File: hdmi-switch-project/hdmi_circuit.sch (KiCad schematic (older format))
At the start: 18 parts, among them U1 TMDS442_single_unit

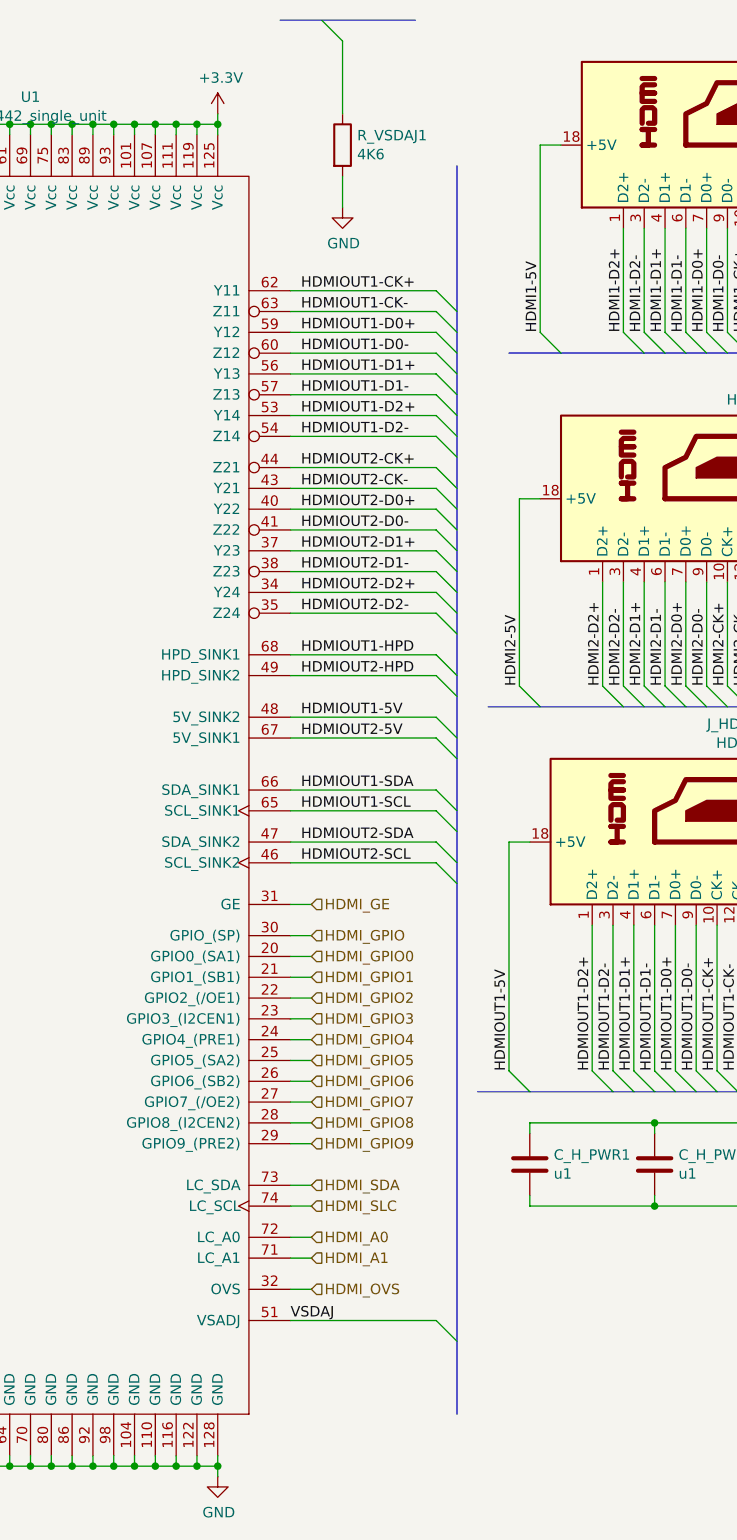
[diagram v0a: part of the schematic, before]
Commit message: Cosmetical changes, and VSDJ pin fixup
Signed-off-by: Andrej Manduch <amanduch@gmail.com>
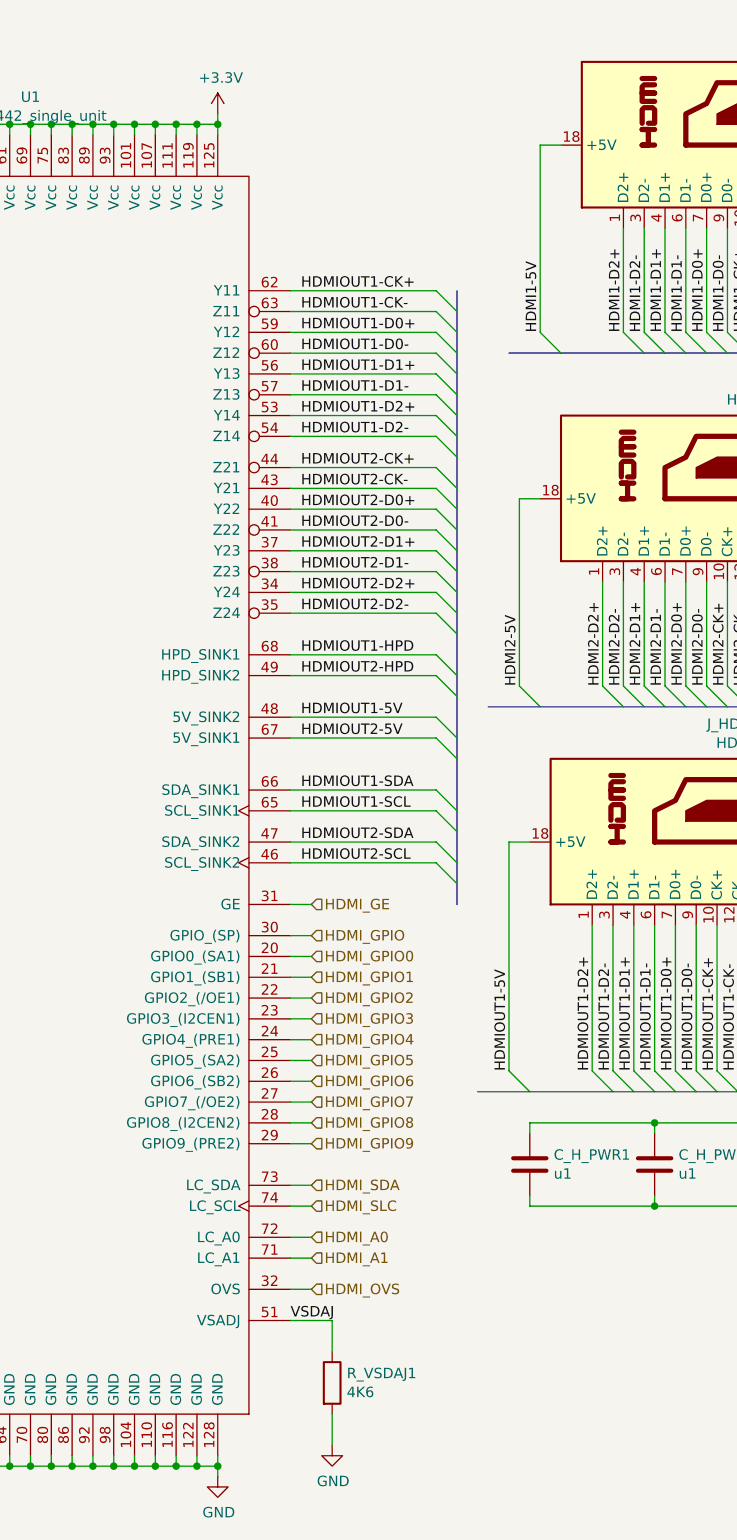
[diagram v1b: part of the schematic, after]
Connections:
- net VSDAJ: now also R_VSDAJ1.1
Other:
- moved on the sheet: R_VSDAJ1
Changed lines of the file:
@@
 encoding utf-8
 Sheet 3 4
-Title ""
-Date ""
+Title "HDMI Switch 4:2 modul"
+Date "2020-06-30"
 Rev ""
 Comp ""
-Comment1 ""
-Comment2 ""
+Comment1 "Devel board"
+Comment2 "HDMI part"
 Comment3 ""
 Comment4 ""
 $EndDescr
 Text GLabel 7400 1450 3    50   Input ~ 0
-SHIELD
-Text GLabel 7300 3150 3    50   Input ~ 0
 SHIELD
 Text GLabel 10200 3100 3    50   Input ~ 0
@@
 Wire Wire Line
 	7300 3050 7300 2950
-Wire Wire Line
-	7300 3150 7300 3050
-Connection ~ 7300 3050
 Wire Wire Line
 	7400 1350 7400 1250
@@
 VSDAJ
 Wire Wire Line
-	3700 6800 4400 6800
+	3700 6800 3900 6800
 Connection ~ 3350 7500
 Wire Wire Line
@@
 Wire Wire Line
 	3350 1050 3350 1000
-Entry Wire Line
-	3850 550  3950 650
-Wire Wire Line
-	3950 650  3950 1000
+Wire Wire Line
+	3900 6800 3900 6950
 $Comp
 L Device:R R_VSDAJ?
 U 1 1 5FA38789
-P 3950 1150
+P 3900 7100
 AR Path="/5FA38789" Ref="R_VSDAJ?"  Part="1"
 AR Path="/5F9FB5DF/5FA38789" Ref="R_VSDAJ1"  Part="1"
-F 0 "R_VSDAJ1" H 4020 1196 50  0000 L CNN
-F 1 "4K6" H 4020 1105 50  0000 L CNN
-F 2 "Resistor_SMD:R_1020_2550Metric" V 3880 1150 50  0001 C CNN
-F 3 "~" H 3950 1150 50  0001 C CNN
-F 4 "Precission" H 3950 1150 50  0001 C CNN "Note"
-	1    3950 1150
+F 0 "R_VSDAJ1" H 3970 7146 50  0000 L CNN
+F 1 "4K6" H 3970 7055 50  0000 L CNN
+F 2 "Resistor_SMD:R_1020_2550Metric" V 3830 7100 50  0001 C CNN
+F 3 "~" H 3900 7100 50  0001 C CNN
+F 4 "Precission" H 3900 7100 50  0001 C CNN "Note"
+	1    3900 7100
 	1    0    0    -1
 $EndComp
@@
 L power:GND #PWR?
 U 1 1 5FA38782
-P 3950 1450
+P 3900 7400
 AR Path="/5FA38782" Ref="#PWR?"  Part="1"
 AR Path="/5F9FB5DF/5FA38782" Ref="#PWR06"  Part="1"
-F 0 "#PWR06" H 3950 1200 50  0001 C CNN
-F 1 "GND" H 3955 1277 50  0000 C CNN
-F 2 "" H 3950 1450 50  0001 C CNN
-F 3 "" H 3950 1450 50  0001 C CNN
-	1    3950 1450
-	1    0    0    -1
-$EndComp
-Wire Wire Line
-	3950 1300 3950 1450
-Entry Wire Line
-	4400 6800 4500 6900
+F 0 "#PWR06" H 3900 7150 50  0001 C CNN
+F 1 "GND" H 3905 7227 50  0000 C CNN
+F 2 "" H 3900 7400 50  0001 C CNN
+F 3 "" H 3900 7400 50  0001 C CNN
+	1    3900 7400
+	1    0    0    -1
+$EndComp
+Wire Wire Line
+	3900 7250 3900 7400
 Connection ~ 10250 6250
 Wire Wire Line
@@
 Connection ~ 9050 5850
 Connection ~ 9050 6250
+Connection ~ 7300 3050
 Wire Bus Line
-	3650 550  4300 550
+	7600 5750 9900 5750
 Wire Bus Line
-	4750 2150 7050 2150
+	550  1500 550  7200
+Wire Bus Line
+	4500 1850 4500 4800
+Wire Bus Line
+	4600 5700 6800 5700
+Wire Bus Line
+	4650 3850 6950 3850
+Wire Bus Line
+	7550 2150 9850 2150
 Wire Bus Line
 	7550 3800 9850 3800
 Wire Bus Line
-	7550 2150 9850 2150
-Wire Bus Line
-	4650 3850 6950 3850
-Wire Bus Line
-	4600 5700 6800 5700
-Wire Bus Line
-	7600 5750 9900 5750
-Wire Bus Line
-	4500 1250 4500 7250
-Wire Bus Line
-	550  1500 550  7200
+	4750 2150 7050 2150
+Wire Wire Line
+	7300 3150 7300 3050
+Text GLabel 7300 3150 3    50   Input ~ 0
+SHIELD
 $EndSCHEMATC

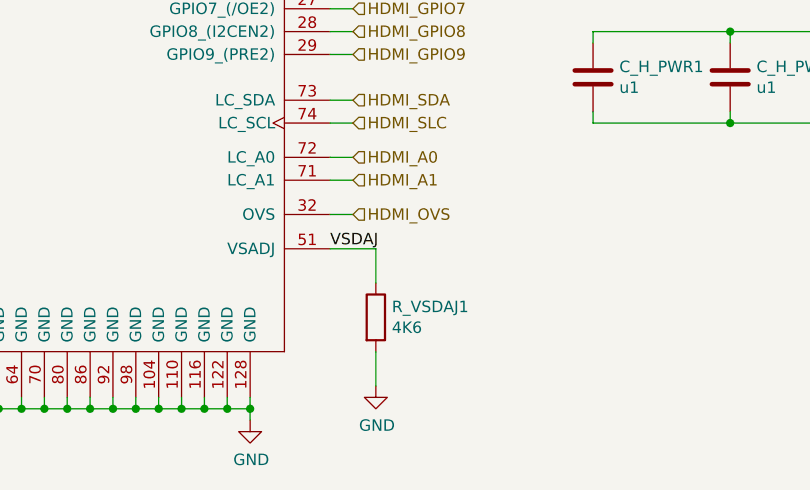
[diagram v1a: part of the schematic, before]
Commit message: Precission resistor changed
from 4k6 to 4k64 %1

Signed-off-by: Andrej Manduch <amanduch@gmail.com>
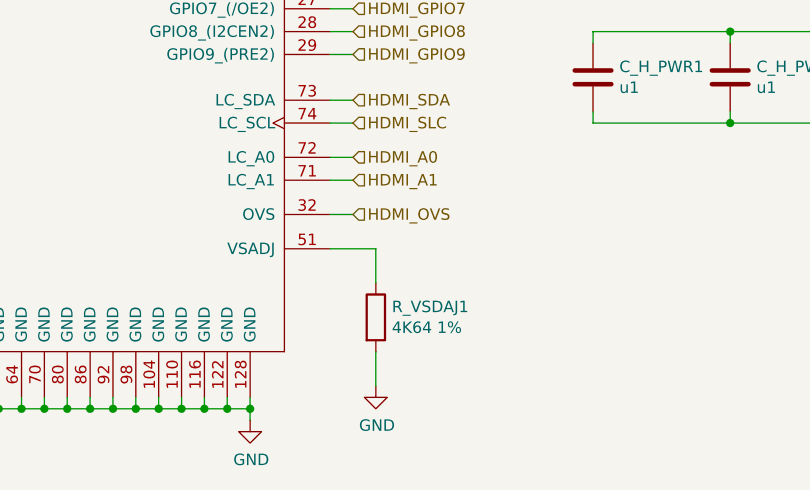
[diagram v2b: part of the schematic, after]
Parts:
- R_VSDAJ1: value 4K6 -> 4K64 1%
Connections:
- net VSDAJ: no longer names the net of R_VSDAJ1.1, U1.51 (VSADJ)
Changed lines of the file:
@@
 Wire Wire Line
 	3800 6500 3700 6500
-Wire Wire Line
-	3700 6650 3800 6650
 Text HLabel 3800 4800 2    50   Input ~ 0
 HDMI_GE
-Text HLabel 3800 6650 2    50   Input ~ 0
-HDMI_OVS
 Text HLabel 3800 6500 2    50   Input ~ 0
 HDMI_A1
@@
 Text HLabel 3800 5050 2    50   Input ~ 0
 HDMI_GPIO0
-$Comp
-L Interface_HDMI:TMDS442_single_unit U?
-U 1 1 5FA3896A
-P 2350 4250
-AR Path="/5FA3896A" Ref="U?"  Part="1"
-AR Path="/5F9FB5DF/5FA3896A" Ref="U1"  Part="1"
-F 0 "U1" H 2450 7581 50  0000 C CNN
-F 1 "TMDS442_single_unit" H 2450 7490 50  0000 C CNN
-F 2 "Package_QFP:TQFP-128_14x14mm_P0.4mm" H 2250 5600 50  0001 C CNN
-F 3 "https://www.ti.com/lit/gpn/tmds442" H 2250 5600 50  0001 C CNN
-	1    2350 4250
-	1    0    0    -1
-$EndComp
 Text HLabel 3800 4950 2    50   Input ~ 0
 HDMI_GPIO
-Text Label 3700 6800 0    50   ~ 0
-VSDAJ
 Wire Wire Line
 	3700 6800 3900 6800
@@
 Wire Wire Line
 	3350 1050 3350 1000
-Wire Wire Line
-	3900 6800 3900 6950
 $Comp
 L Device:R R_VSDAJ?
@@
 AR Path="/5F9FB5DF/5FA38789" Ref="R_VSDAJ1"  Part="1"
 F 0 "R_VSDAJ1" H 3970 7146 50  0000 L CNN
-F 1 "4K6" H 3970 7055 50  0000 L CNN
+F 1 "4K64 1%" H 3970 7055 50  0000 L CNN
 F 2 "Resistor_SMD:R_1020_2550Metric" V 3830 7100 50  0001 C CNN
 F 3 "~" H 3900 7100 50  0001 C CNN
@@
 Connection ~ 9050 6250
 Connection ~ 7300 3050
+Wire Wire Line
+	7300 3150 7300 3050
+Text GLabel 7300 3150 3    50   Input ~ 0
+SHIELD
 Wire Bus Line
 	7600 5750 9900 5750
@@
 	4750 2150 7050 2150
 Wire Wire Line
-	7300 3150 7300 3050
-Text GLabel 7300 3150 3    50   Input ~ 0
-SHIELD
+	3900 6800 3900 6950
+$Comp
+L Interface_HDMI:TMDS442_single_unit U?
+U 1 1 5FA3896A
+P 2350 4250
+AR Path="/5FA3896A" Ref="U?"  Part="1"
+AR Path="/5F9FB5DF/5FA3896A" Ref="U1"  Part="1"
+F 0 "U1" H 2450 7581 50  0000 C CNN
+F 1 "TMDS442_single_unit" H 2450 7490 50  0000 C CNN
+F 2 "Package_QFP:TQFP-128_14x14mm_P0.4mm" H 2250 5600 50  0001 C CNN
+F 3 "https://www.ti.com/lit/gpn/tmds442" H 2250 5600 50  0001 C CNN
+	1    2350 4250
+	1    0    0    -1
+$EndComp
+Text HLabel 3800 6650 2    50   Input ~ 0
+HDMI_OVS
+Wire Wire Line
+	3700 6650 3800 6650
 $EndSCHEMATC

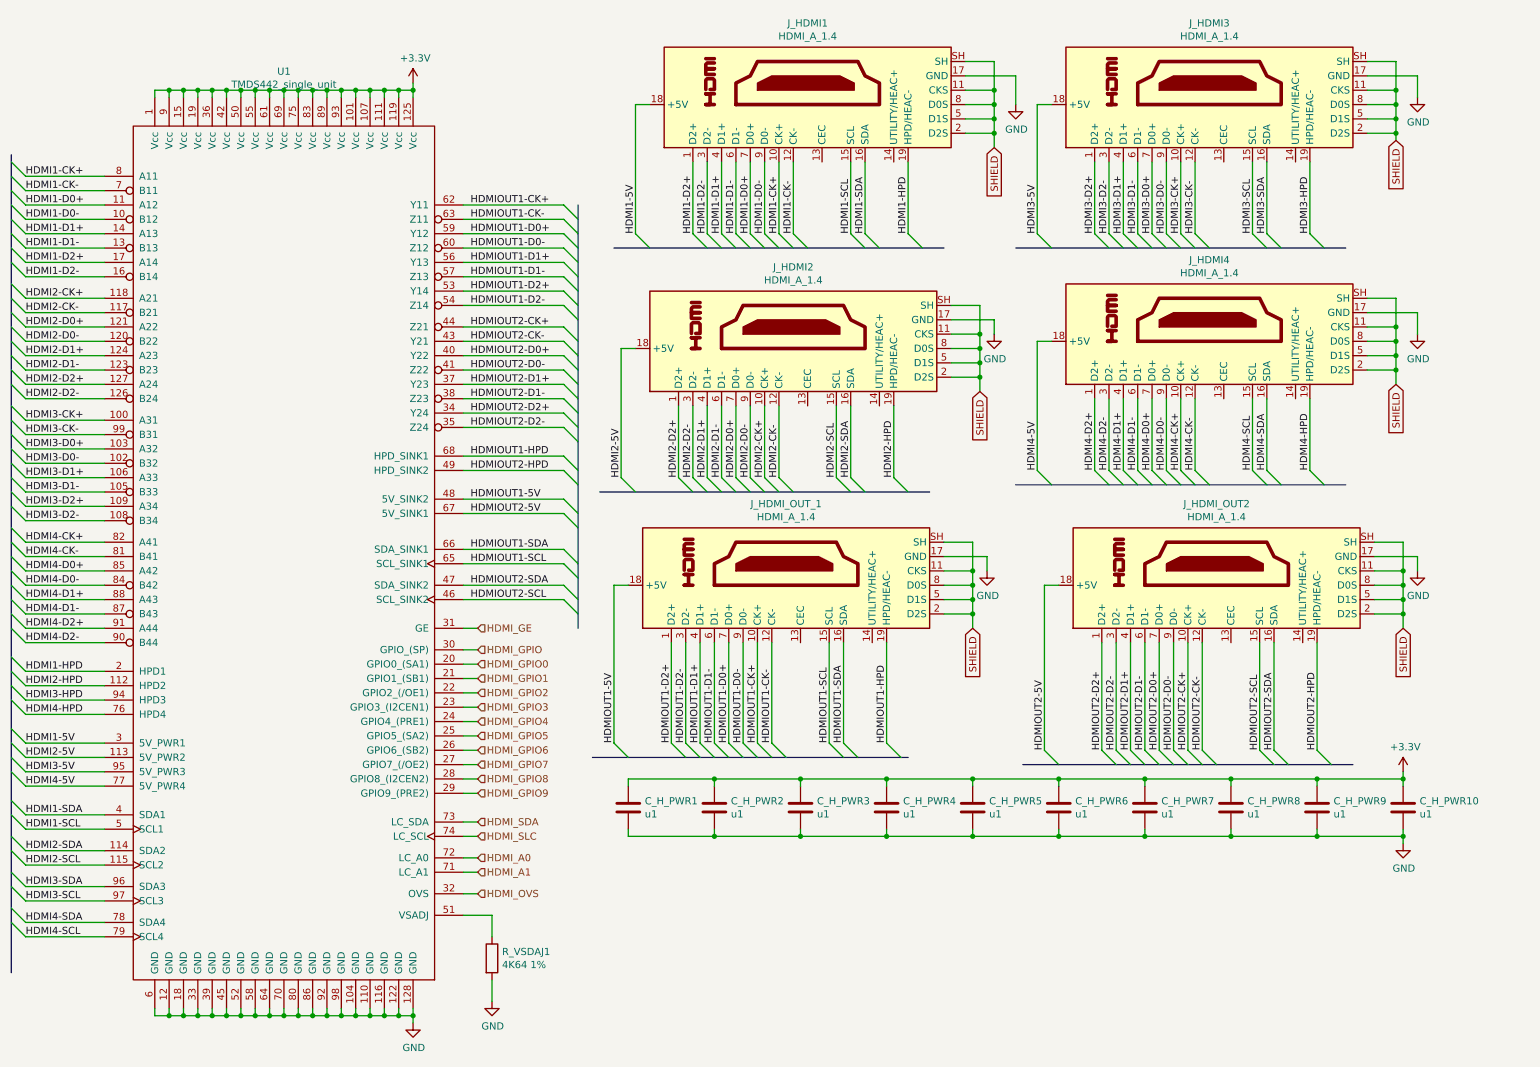
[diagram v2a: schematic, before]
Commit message: Added terminal resistors for HDMI I2C
Signed-off-by: Andrej Manduch <amanduch@gmail.com>
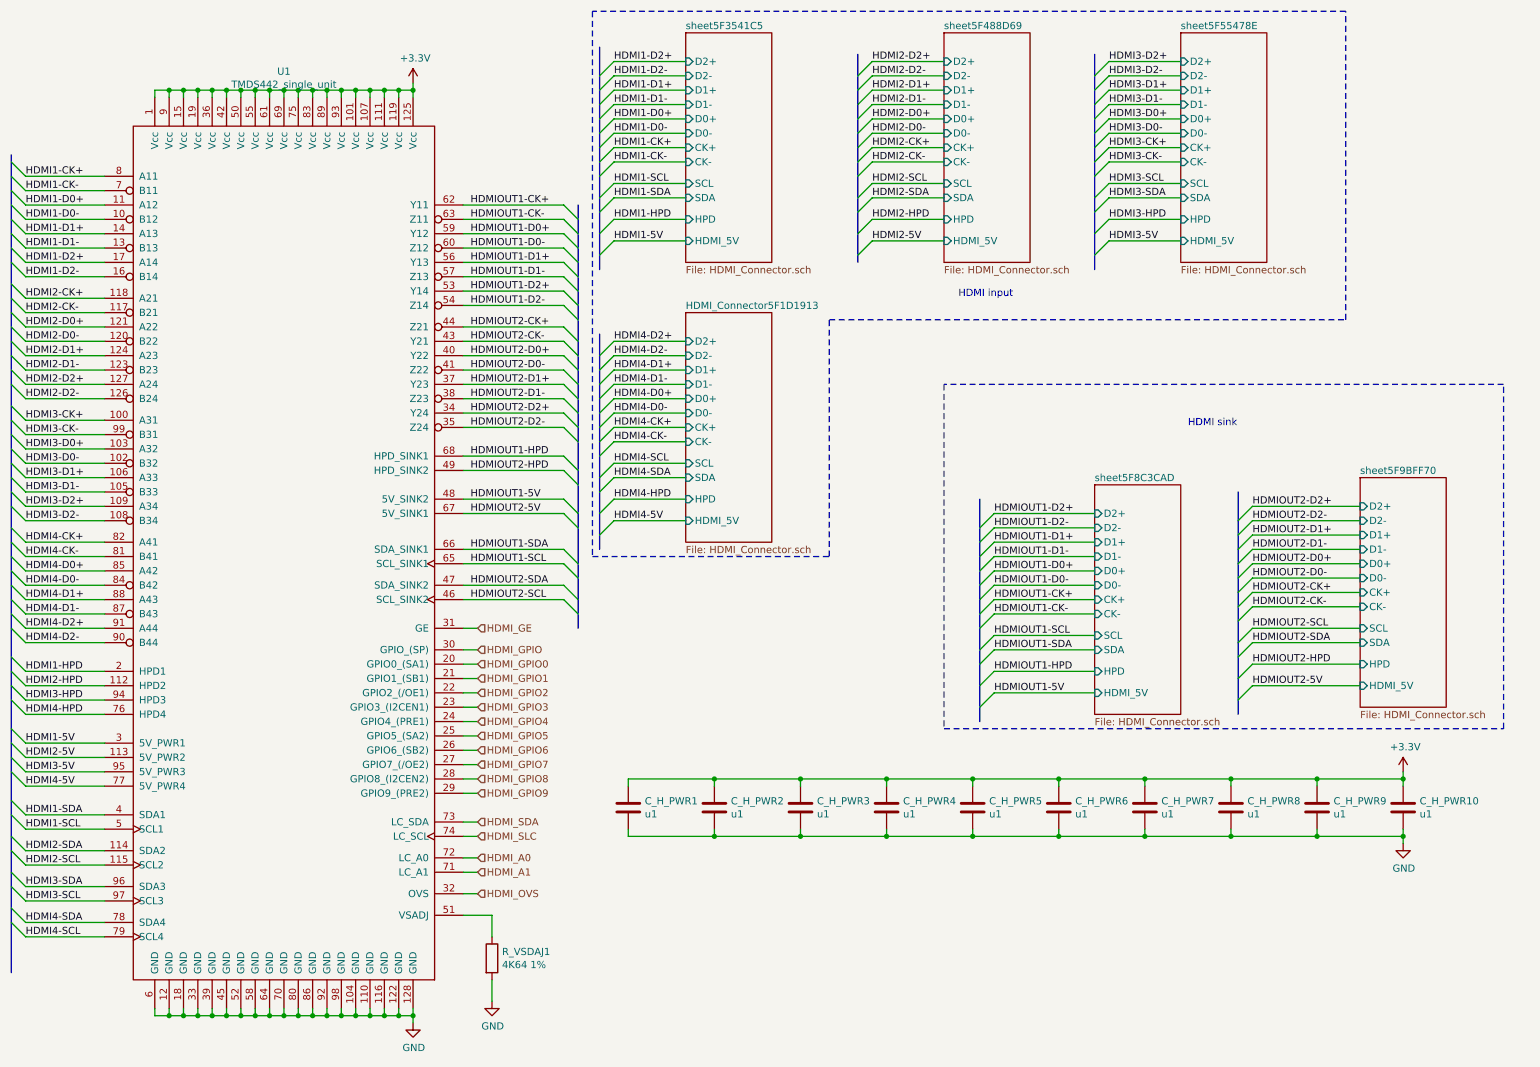
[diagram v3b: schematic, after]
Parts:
- removed J_HDMI1, J_HDMI2, J_HDMI3, J_HDMI4, J_HDMI_OUT2, J_HDMI_OUT_1: HDMI_A_1.4, Connector_HDMI:HDMI_A_Contact_Technology_HDMI-19APL2_Horizontal, symbol Connector:HDMI_A_1.4
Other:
- note added: "HDMI input"
- note added: "HDMI sink"
